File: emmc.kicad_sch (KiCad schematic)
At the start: 0 parts

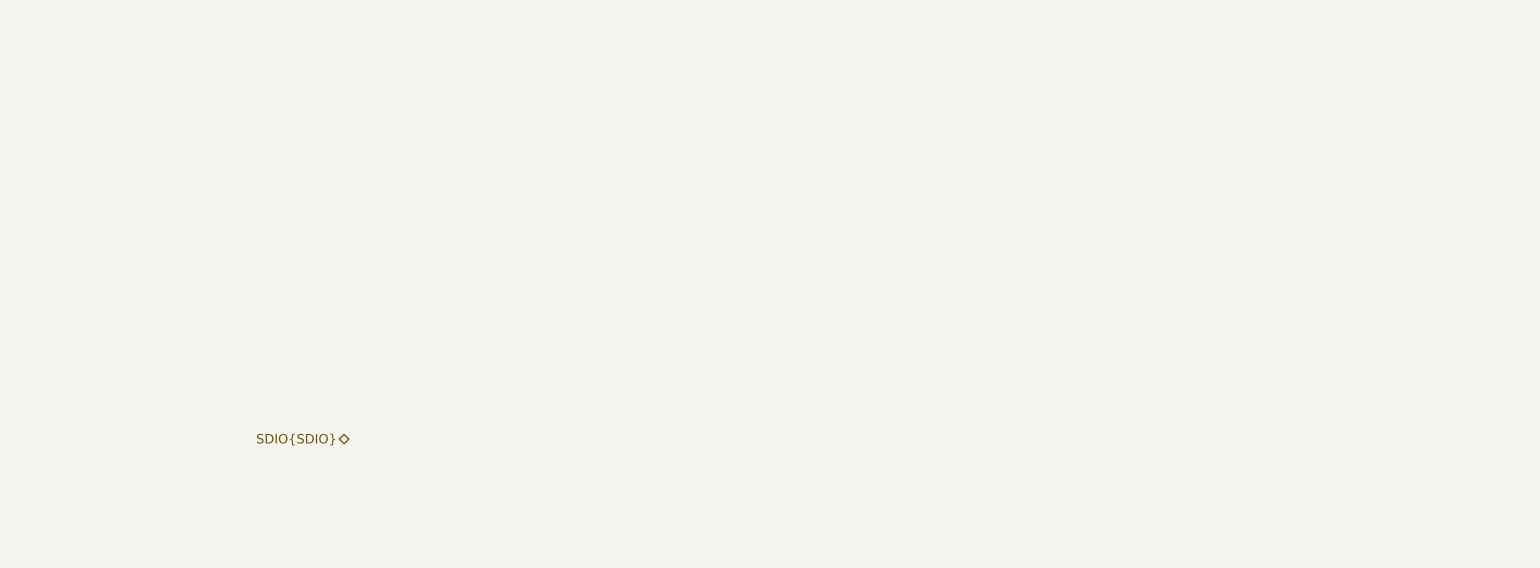
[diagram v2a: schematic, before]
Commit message: [#82176] Add placeholder eMMC
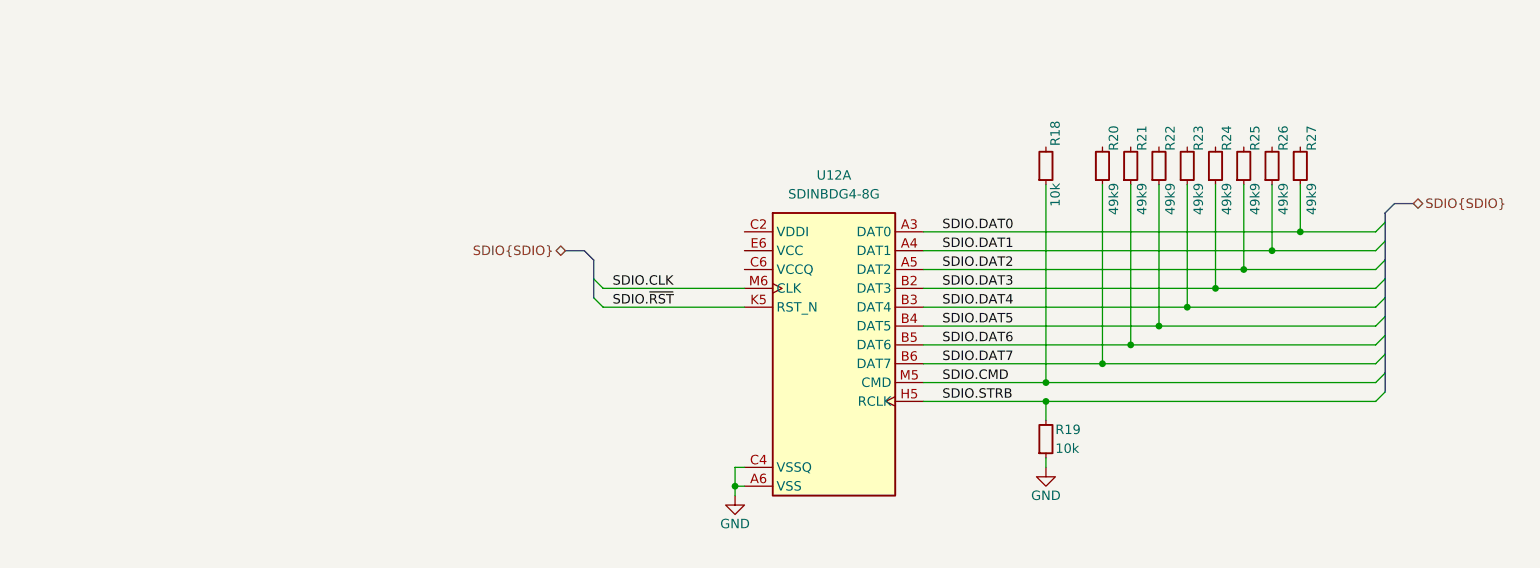
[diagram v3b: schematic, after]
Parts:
- added R18, R19: R_10k_0402, antmicro-footprints:R_0402_1005Metric, symbol antmicroResistors0402:R_10k_0402
- added R20, R21, R22, R23, R24, R25, R26, R27: R_49k9_0402, antmicro-footprints:R_0402_1005Metric, symbol antmicroResistors0402:R_49k9_0402
- added U12: SDINBDG4-8G, antmicro-footprints:BGA-196-153_11.5x13mm_Layout14x14_P0.5x0.5mm, symbol antmicroMemory:SDINBDG4-8G
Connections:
- new net: U12.C6 (VCCQ), U12.M4 (VCCQ), U12.N4 (VCCQ), U12.P3 (VCCQ), U12.P5 (VCCQ)
- new net: U12.E6 (VCC), U12.F5 (VCC), U12.J10 (VCC), U12.K9 (VCC)
- new net GND: R19.1, U12.A6 (VSS), U12.C4 (VSSQ), U12.E7 (VSS), U12.G5 (VSS), U12.H10 (VSS), U12.J5 (VSS), U12.K8 (VSS), U12.N2 (VSSQ), U12.N5 (VSSQ), U12.P4 (VSSQ), U12.P6 (VSSQ)
- new net SDIO.CLK: U12.M6 (CLK)
- new net SDIO.CMD: R18.1, U12.M5 (CMD)
- new net SDIO.DAT0: R27.1, U12.A3 (DAT0)
- new net SDIO.DAT1: R26.1, U12.A4 (DAT1)
- new net SDIO.DAT2: R25.1, U12.A5 (DAT2)
- new net SDIO.DAT3: R24.1, U12.B2 (DAT3)
- new net SDIO.DAT4: R23.1, U12.B3 (DAT4)
- new net SDIO.DAT5: R22.1, U12.B4 (DAT5)
- new net SDIO.DAT6: R21.1, U12.B5 (DAT6)
- new net SDIO.DAT7: R20.1, U12.B6 (DAT7)
- new net SDIO.STRB: R19.2, U12.H5 (RCLK)
- new net SDIO.~{RST}: U12.K5 (RST_N)

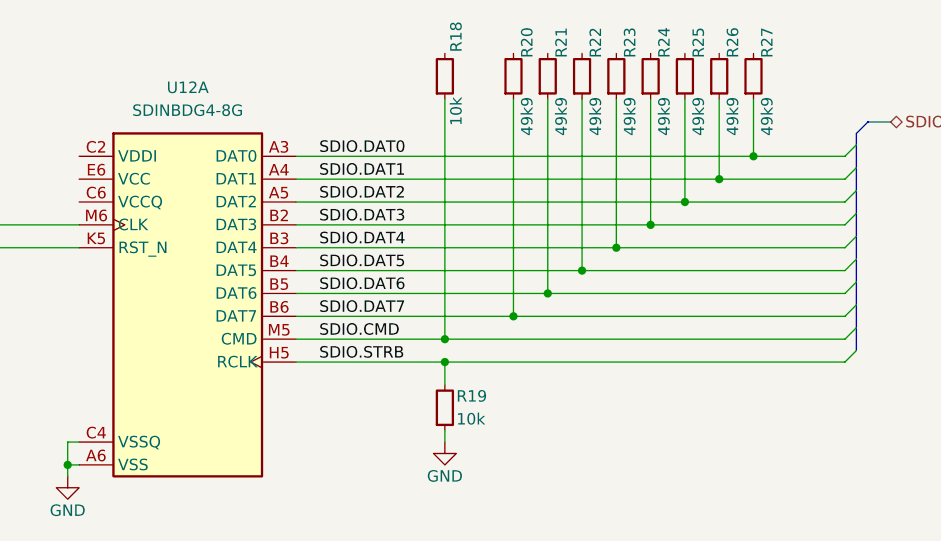
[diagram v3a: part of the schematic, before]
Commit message: [#82176] Fix conflicting annotations
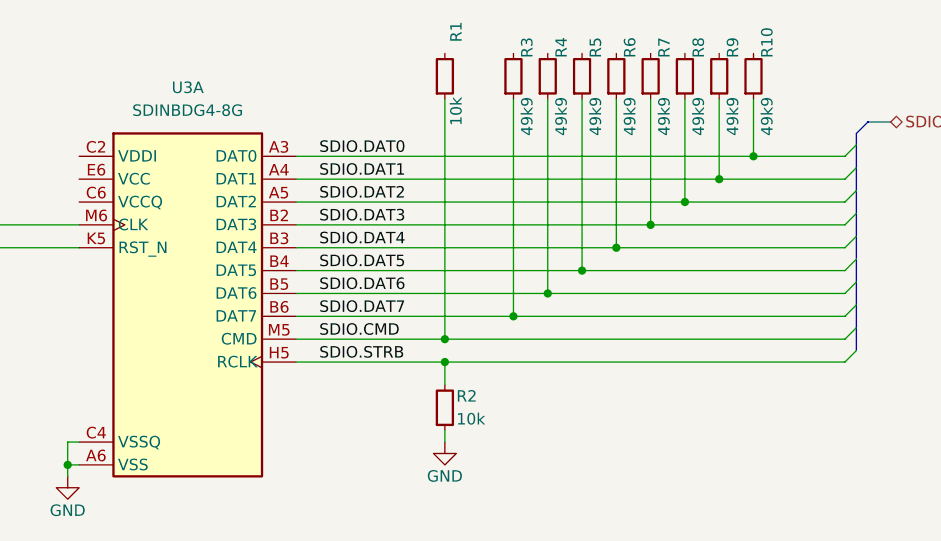
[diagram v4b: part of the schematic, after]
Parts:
- renumbered R18 to R1, R27 to R10, R19 to R2, R20 to R3, R21 to R4, R22 to R5, R23 to R6, R24 to R7, R25 to R8, R26 to R9, U12 to U3
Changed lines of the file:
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@@
 		(on_board yes)
 		(dnp no)
-		(property "Reference" "#PWR024"
+		(property "Reference" "#PWR03"
 			(at 245.11 151.13 0)
 			(effects
@@
 			(project "bmc-reference-carrier-board"
 				(path "/5f636c45-3c15-4731-8931-4625e0dab7e4/af9b114c-dfa4-427f-a7c0-6a1753518223"
-					(reference "#PWR024")
+					(reference "#PWR03")
 					(unit 1)
 				)
@@
 		(on_board yes)
 		(dnp no)
-		(property "Reference" "R20"
+		(property "Reference" "R3"
 			(at 245.364 105.918 0)
 			(effects
@@
 			(project ""
 				(path "/5f636c45-3c15-4731-8931-4625e0dab7e4/af9b114c-dfa4-427f-a7c0-6a1753518223"
-					(reference "R20")
+					(reference "R3")
 					(unit 1)
 				)
@@
 		(on_board yes)
 		(dnp no)
-		(property "Reference" "R24"
+		(property "Reference" "R7"
 			(at 260.604 105.918 0)
 			(effects
@@
 			(project "bmc-reference-carrier-board"
 				(path "/5f636c45-3c15-4731-8931-4625e0dab7e4/af9b114c-dfa4-427f-a7c0-6a1753518223"
-					(reference "R24")
+					(reference "R7")
 					(unit 1)
 				)
@@
 		(on_board yes)
 		(dnp no)
-		(property "Reference" "R23"
+		(property "Reference" "R6"
 			(at 256.794 105.918 0)
 			(effects
@@
 			(project "bmc-reference-carrier-board"
 				(path "/5f636c45-3c15-4731-8931-4625e0dab7e4/af9b114c-dfa4-427f-a7c0-6a1753518223"
-					(reference "R23")
+					(reference "R6")
 					(unit 1)
 				)
@@
 		(on_board yes)
 		(dnp no)
-		(property "Reference" "R21"
+		(property "Reference" "R4"
 			(at 249.174 105.918 0)
 			(effects
@@
 			(project "bmc-reference-carrier-board"
 				(path "/5f636c45-3c15-4731-8931-4625e0dab7e4/af9b114c-dfa4-427f-a7c0-6a1753518223"
-					(reference "R21")
+					(reference "R4")
 					(unit 1)
 				)
@@
 		(on_board yes)
 		(dnp no)
-		(property "Reference" "R22"
+		(property "Reference" "R5"
 			(at 252.984 105.918 0)
 			(effects
@@
 			(project "bmc-reference-carrier-board"
 				(path "/5f636c45-3c15-4731-8931-4625e0dab7e4/af9b114c-dfa4-427f-a7c0-6a1753518223"
-					(reference "R22")
+					(reference "R5")
 					(unit 1)
 				)
@@
 		(on_board yes)
 		(dnp no)
-		(property "Reference" "#PWR023"
+		(property "Reference" "#PWR02"
 			(at 203.2 154.94 0)
 			(effects
@@
 			(project "bmc-reference-carrier-board"
 				(path "/5f636c45-3c15-4731-8931-4625e0dab7e4/af9b114c-dfa4-427f-a7c0-6a1753518223"
-					(reference "#PWR023")
+					(reference "#PWR02")
 					(unit 1)
 				)
@@
 		(on_board yes)
 		(dnp no)
-		(property "Reference" "R18"
+		(property "Reference" "R1"
 			(at 237.49 101.854 0)
 			(effects
@@
 			(project "bmc-reference-carrier-board"
 				(path "/5f636c45-3c15-4731-8931-4625e0dab7e4/af9b114c-dfa4-427f-a7c0-6a1753518223"
-					(reference "R18")
+					(reference "R1")
 					(unit 1)
 				)
@@
 		(dnp no)
 		(fields_autoplaced yes)
-		(property "Reference" "U12"
+		(property "Reference" "U3"
 			(at 207.645 109.22 0)
 			(effects
@@
 			(project ""
 				(path "/5f636c45-3c15-4731-8931-4625e0dab7e4/af9b114c-dfa4-427f-a7c0-6a1753518223"
-					(reference "U12")
+					(reference "U3")
 					(unit 1)
 				)
@@
 		(on_board yes)
 		(dnp no)
-		(property "Reference" "R25"
+		(property "Reference" "R8"
 			(at 264.414 105.918 0)
 			(effects
@@
 			(project "bmc-reference-carrier-board"
 				(path "/5f636c45-3c15-4731-8931-4625e0dab7e4/af9b114c-dfa4-427f-a7c0-6a1753518223"
-					(reference "R25")
+					(reference "R8")
 					(unit 1)
 				)
@@
 		(on_board yes)
 		(dnp no)
-		(property "Reference" "R27"
+		(property "Reference" "R10"
 			(at 272.034 105.918 0)
 			(effects
@@
 			(project "bmc-reference-carrier-board"
 				(path "/5f636c45-3c15-4731-8931-4625e0dab7e4/af9b114c-dfa4-427f-a7c0-6a1753518223"
-					(reference "R27")
+					(reference "R10")
 					(unit 1)
 				)
@@
 		(on_board yes)
 		(dnp no)
-		(property "Reference" "R19"
+		(property "Reference" "R2"
 			(at 237.49 143.51 90)
 			(effects
@@
 			(project "bmc-reference-carrier-board"
 				(path "/5f636c45-3c15-4731-8931-4625e0dab7e4/af9b114c-dfa4-427f-a7c0-6a1753518223"
-					(reference "R19")
+					(reference "R2")
 					(unit 1)
 				)
@@
 		(on_board yes)
 		(dnp no)
-		(property "Reference" "R26"
+		(property "Reference" "R9"
 			(at 268.224 105.918 0)
 			(effects
@@
 			(project "bmc-reference-carrier-board"
 				(path "/5f636c45-3c15-4731-8931-4625e0dab7e4/af9b114c-dfa4-427f-a7c0-6a1753518223"
-					(reference "R26")
+					(reference "R9")
 					(unit 1)
 				)

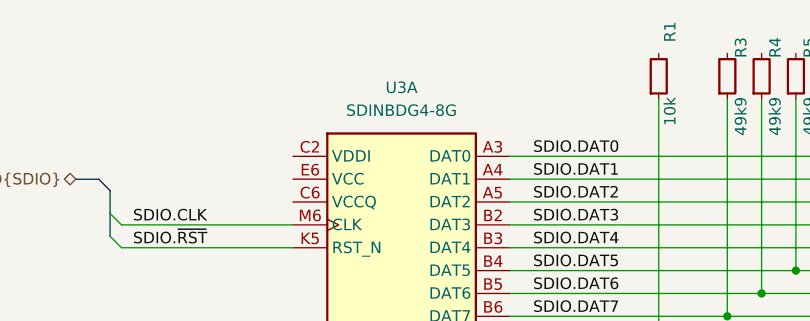
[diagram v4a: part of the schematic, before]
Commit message: [#82323] Connect OSM signals
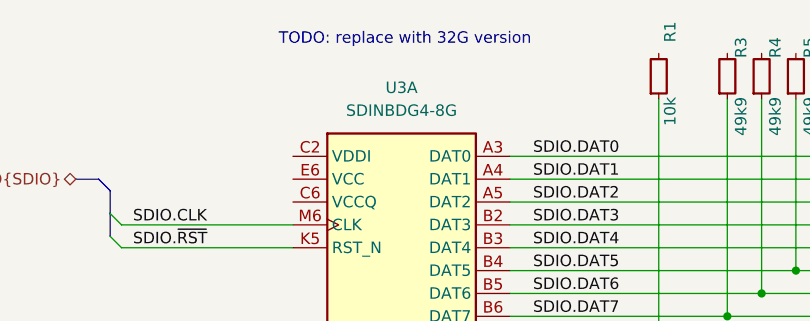
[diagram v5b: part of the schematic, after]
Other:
- note added: "TODO: replace with 32G version"
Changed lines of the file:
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@@
 		(rev "1.0.0")
+	)
+	(text "TODO: replace with 32G version"
+		(exclude_from_sim no)
+		(at 208.026 103.886 0)
+		(effects
+			(font
+				(size 1.27 1.27)
+			)
+		)
 	)
 	(junction

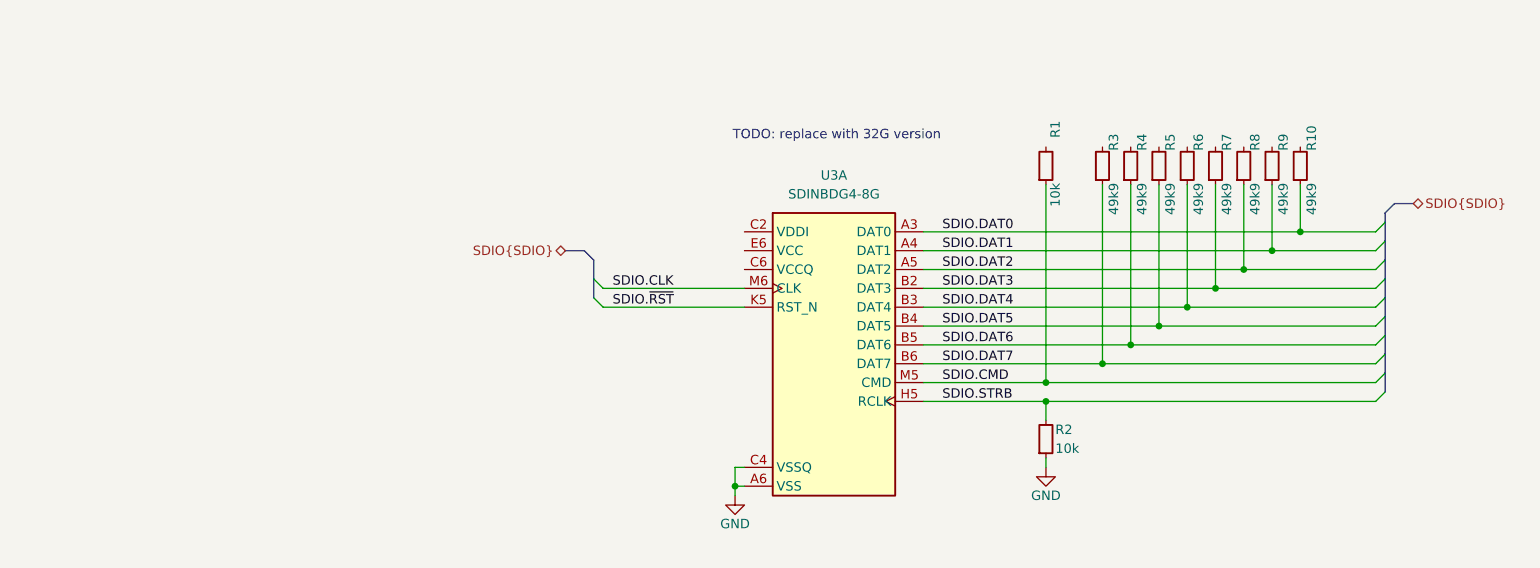
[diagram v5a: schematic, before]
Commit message: [#82176] eMMC: change chip to 32GB & add decoupling
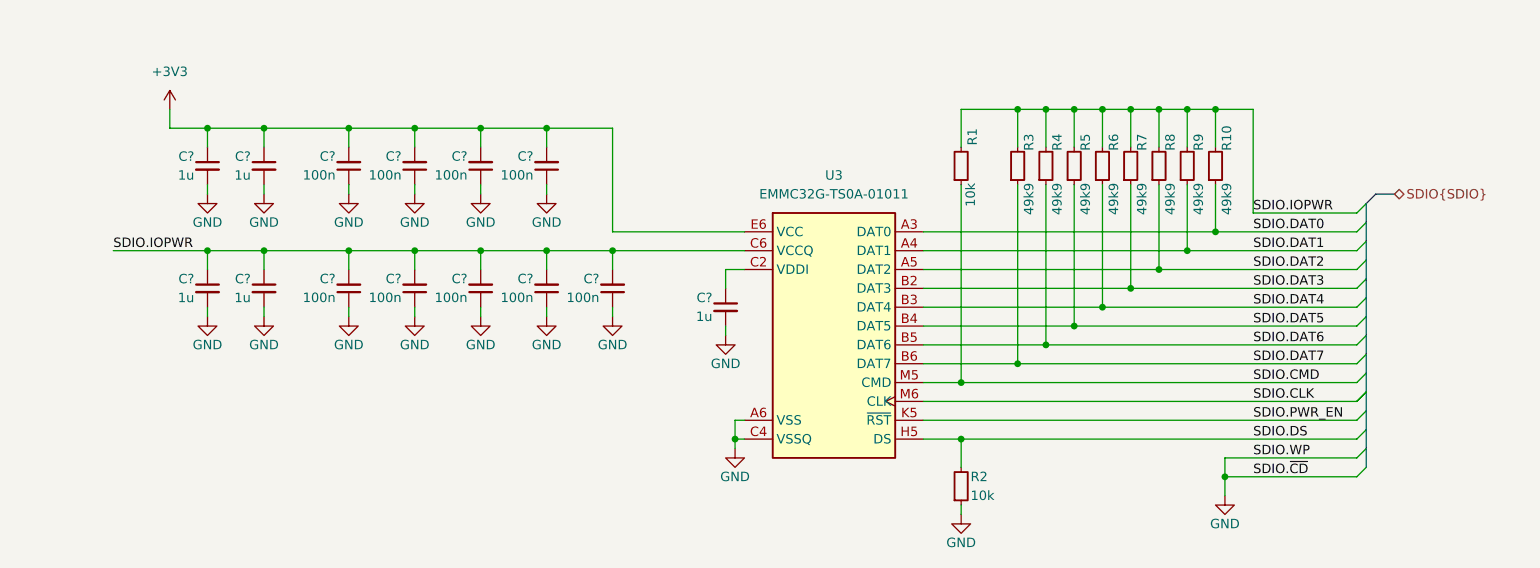
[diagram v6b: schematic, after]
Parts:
- added C? (x9): C_100n_0402, antmicro-footprints:C_0402_1005Metric, symbol antmicroCapacitors0402:C_100n_0402
- added C? (x5): C_1u_0402, antmicro-footprints:C_0402_1005Metric, symbol antmicroCapacitors0402:C_1u_0402
- U3: value SDINBDG4-8G -> EMMC32G-TS0A-01011; footprint antmicro-footprints:BGA-196-153_11.5x13mm_Layout14x14_P0.5x0.5mm -> antmicro-footprints:BGA-196-153_10x11mm_Layout14x14_P0.5x0.5mm; symbol antmicroMemory:SDINBDG4-8G -> antmicroMemory:EMMC32G-TS0A-01011; MPN SDINBDG4-8G -> EMMC32G-TS0A-01011; Manufacturer SanDisk -> Kingston
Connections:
- net GND: now also C?.1, C?.1, C?.1, C?.1, C?.1, C?.1, C?.1, C?.1, C?.1, C?.2, C?.2, C?.2, C?.2, C?.2
- net SDIO.IOPWR: now reaches R3.2
- net SDIO.IOPWR: now also R1.2, R10.2, R4.2, R5.2, R6.2, R7.2, R8.2, R9.2, U3.C6 (VCCQ), U3.M4 (VCCQ), U3.N4 (VCCQ), U3.P3 (VCCQ), U3.P5 (VCCQ), C?.1, C?.1, C?.2, C?.2, C?.2, C?.2, C?.2
- net at U3.A7 (RFU): now also U3.E5 (RFU), U3.E8 (RFU), U3.G10 (RFU), U3.G3 (RFU), U3.K10 (RFU), U3.K6 (RFU), U3.K7 (RFU), U3.P10 (RFU), U3.P7 (RFU)
- net at U3.C2 (VDDI): now also C?.1
- net at U3.E10 (VSF): now also U3.E9 (VSF), U3.F10 (VSF)
- net +3V3: now reaches U3.E6 (VCC), U3.F5 (VCC), U3.J10 (VCC), U3.K9 (VCC)
- net +3V3: now also C?.1, C?.1, C?.2, C?.2, C?.2, C?.2
- net SDIO.STRB renamed SDIO.DS
- net SDIO.~{RST} renamed SDIO.PWR_EN
- new net: U3.A1 (NC), U3.A10 (NC), U3.A11 (NC), U3.A12 (NC), U3.A13 (NC), U3.A14 (NC), U3.A2 (NC), U3.A8 (NC), U3.A9 (NC), U3.B1 (NC), U3.B10 (NC), U3.B11 (NC), U3.B12 (NC), U3.B13 (NC), U3.B14 (NC), U3.B7 (NC), U3.B8 (NC), U3.B9 (NC), U3.C1 (NC), U3.C10 (NC), U3.C11 (NC), U3.C12 (NC), U3.C13 (NC), U3.C14 (NC), U3.C3 (NC), U3.C5 (NC), U3.C7 (NC), U3.C8 (NC), U3.C9 (NC), U3.D1 (NC), U3.D12 (NC), U3.D13 (NC), U3.D14 (NC), U3.D2 (NC), U3.D3 (NC), U3.D4 (NC), U3.E1 (NC), U3.E12 (NC), U3.E13 (NC), U3.E14 (NC), U3.E2 (NC), U3.E3 (NC), U3.F1 (NC), U3.F12 (NC), U3.F13 (NC), U3.F14 (NC), U3.F2 (NC), U3.F3 (NC), U3.G1 (NC), U3.G12 (NC), U3.G13 (NC), U3.G14 (NC), U3.G2 (NC), U3.H1 (NC), U3.H12 (NC), U3.H13 (NC), U3.H14 (NC), U3.H2 (NC), U3.H3 (NC), U3.J1 (NC), U3.J12 (NC), U3.J13 (NC), U3.J14 (NC), U3.J2 (NC), U3.J3 (NC), U3.K1 (NC), U3.K12 (NC), U3.K13 (NC), U3.K14 (NC), U3.K2 (NC), U3.K3 (NC), U3.L1 (NC), U3.L12 (NC), U3.L13 (NC), U3.L14 (NC), U3.L2 (NC), U3.L3 (NC), U3.M1 (NC), U3.M10 (NC), U3.M11 (NC), U3.M12 (NC), U3.M13 (NC), U3.M14 (NC), U3.M2 (NC), U3.M3 (NC), U3.M7 (NC), U3.M8 (NC), U3.M9 (NC), U3.N1 (NC), U3.N10 (NC), U3.N11 (NC), U3.N12 (NC), U3.N13 (NC), U3.N14 (NC), U3.N3 (NC), U3.N6 (NC), U3.N7 (NC), U3.N8 (NC), U3.N9 (NC), U3.P1 (NC), U3.P11 (NC), U3.P12 (NC), U3.P13 (NC), U3.P14 (NC), U3.P2 (NC), U3.P8 (NC), U3.P9 (NC)
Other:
- note removed: "TODO: replace with 32G version"
- moved on the sheet: R1, R10, R2, R3, R4, R5, R6, R7, R8, R9

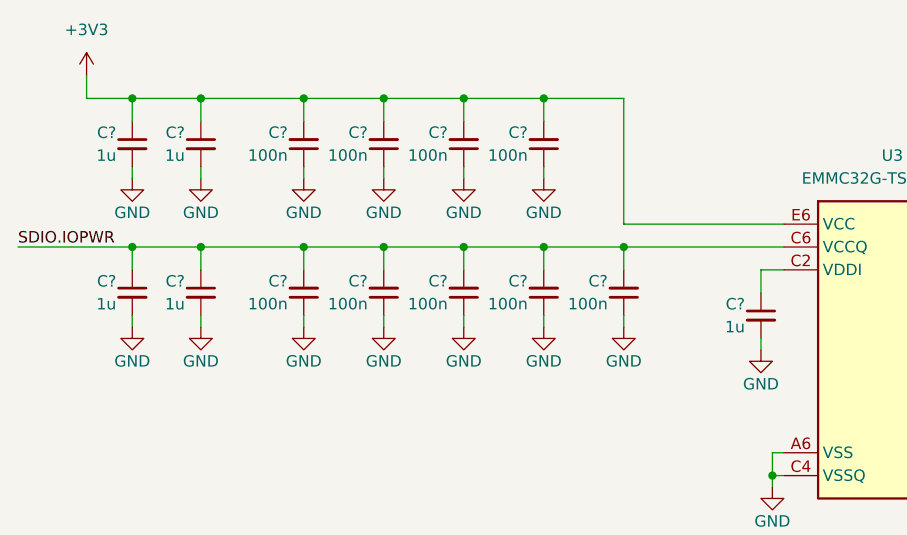
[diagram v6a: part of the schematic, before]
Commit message: [#82176] Connect eMMC SDIO to OSM, annotate eMMC schematic
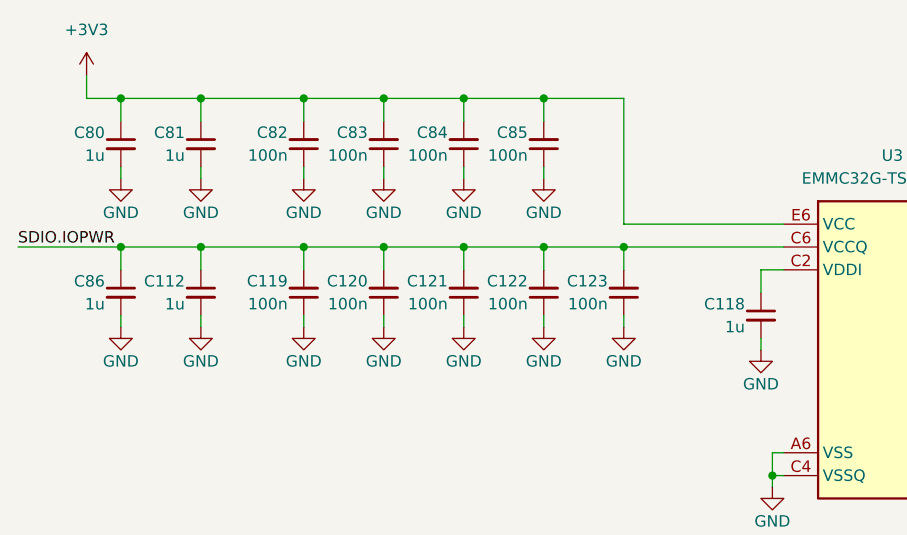
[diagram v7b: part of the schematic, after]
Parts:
- gave numbers to parts that had none: 14
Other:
- moved on the sheet: C80, C86

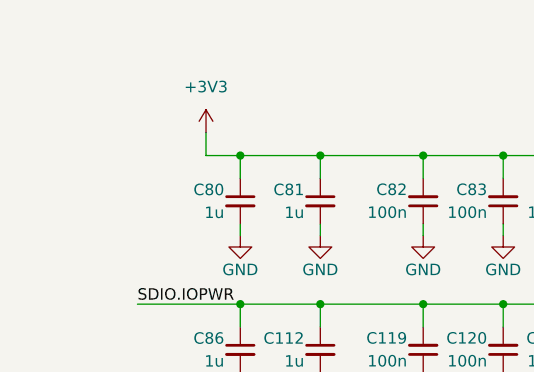
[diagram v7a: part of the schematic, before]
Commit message: [#83609] Connect PWR_EN signal, change eMMC power to AON, minor schematic refactor
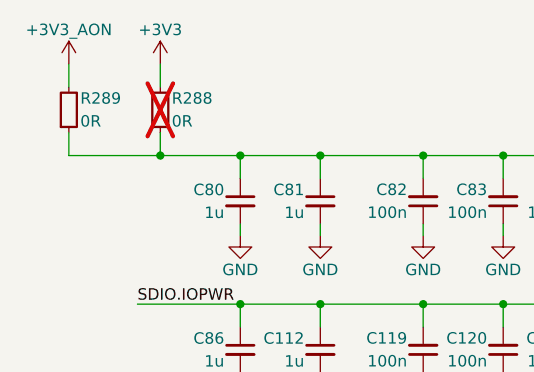
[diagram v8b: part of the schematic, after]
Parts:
- added R288, R289: R_0R_0402, antmicro-footprints:R_0402_1005Metric, symbol antmicroResistors0402:R_0R_0402
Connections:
- net +3V3: now also R288.2; no longer C80.1, C81.1, C82.2, C83.2, C84.2, C85.2, U3.E6 (VCC), U3.F5 (VCC), U3.J10 (VCC), U3.K9 (VCC)
- new net: C80.1, C81.1, C82.2, C83.2, C84.2, C85.2, R288.1, R289.1, U3.E6 (VCC), U3.F5 (VCC), U3.J10 (VCC), U3.K9 (VCC)
- new net +3V3_AON: R289.2
